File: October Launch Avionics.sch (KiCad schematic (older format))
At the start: 18 parts, among them IC1 MPU-6050, IC2 790, IC3 BMP384, J1 U.FL-R-SMT_01_, J2 MEM2075-00-140-01-A, U1 ESP32-WROOM-32D

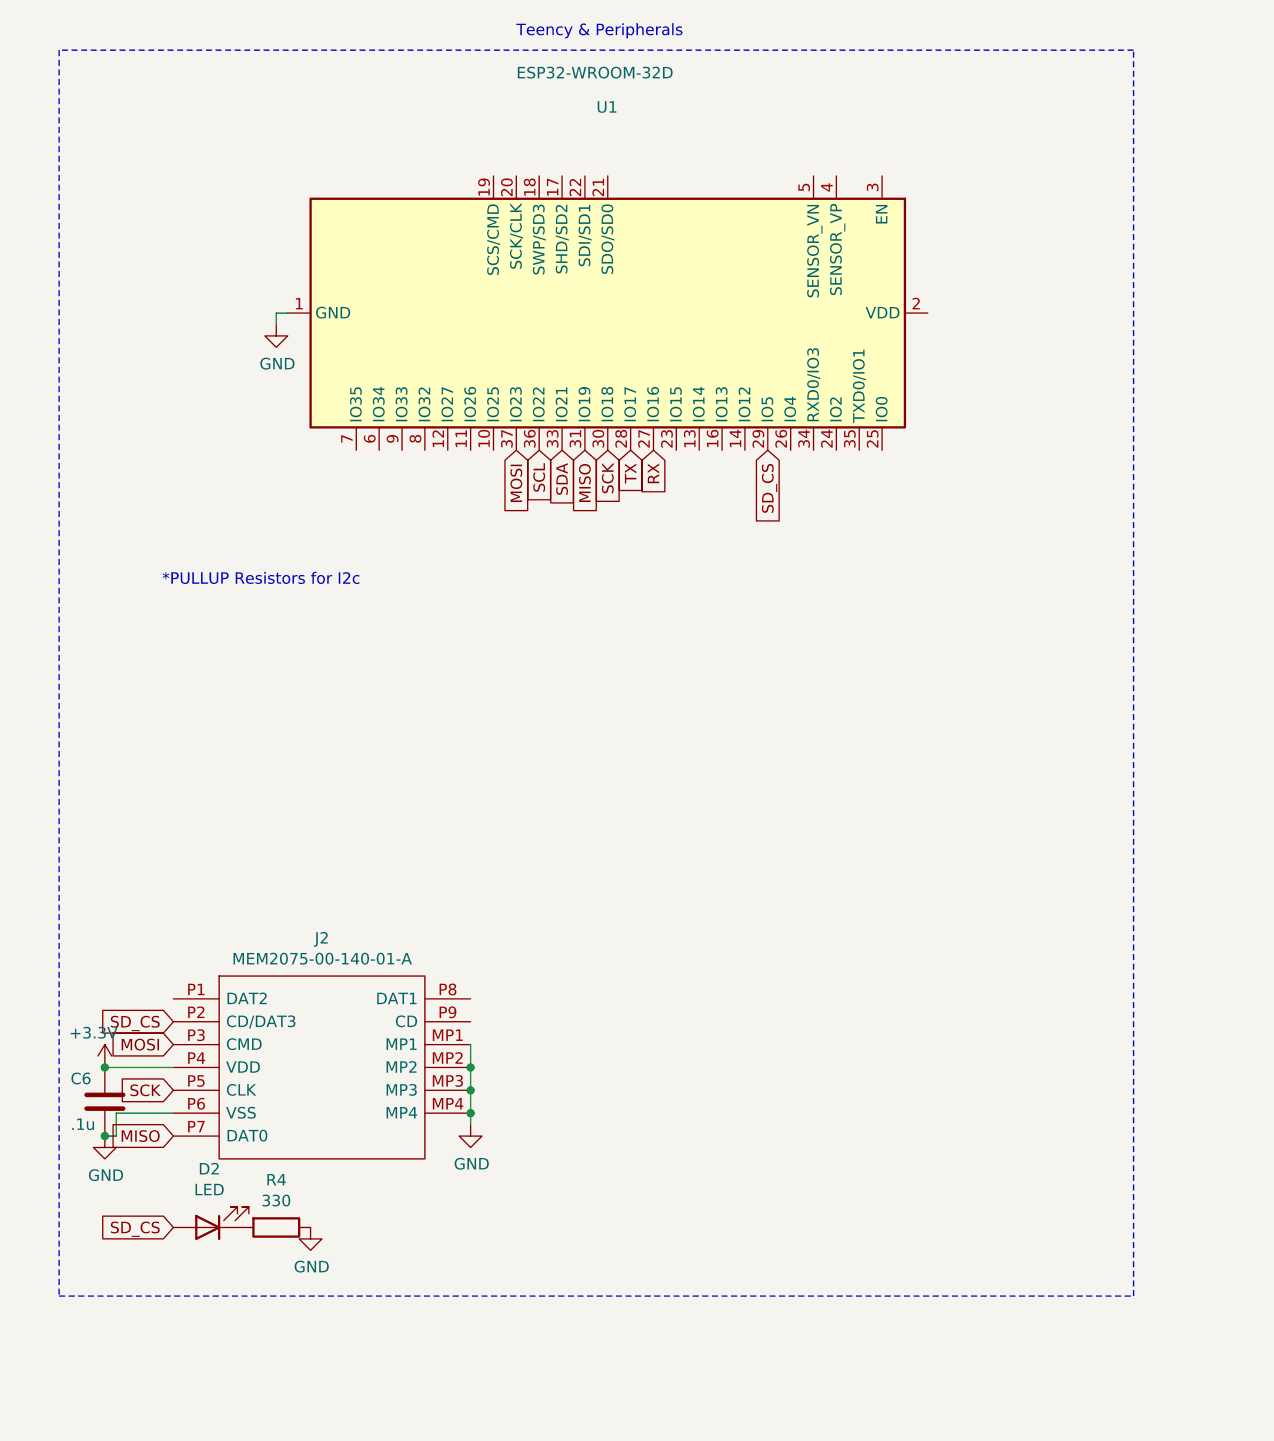
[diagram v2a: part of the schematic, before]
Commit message: Added reset button
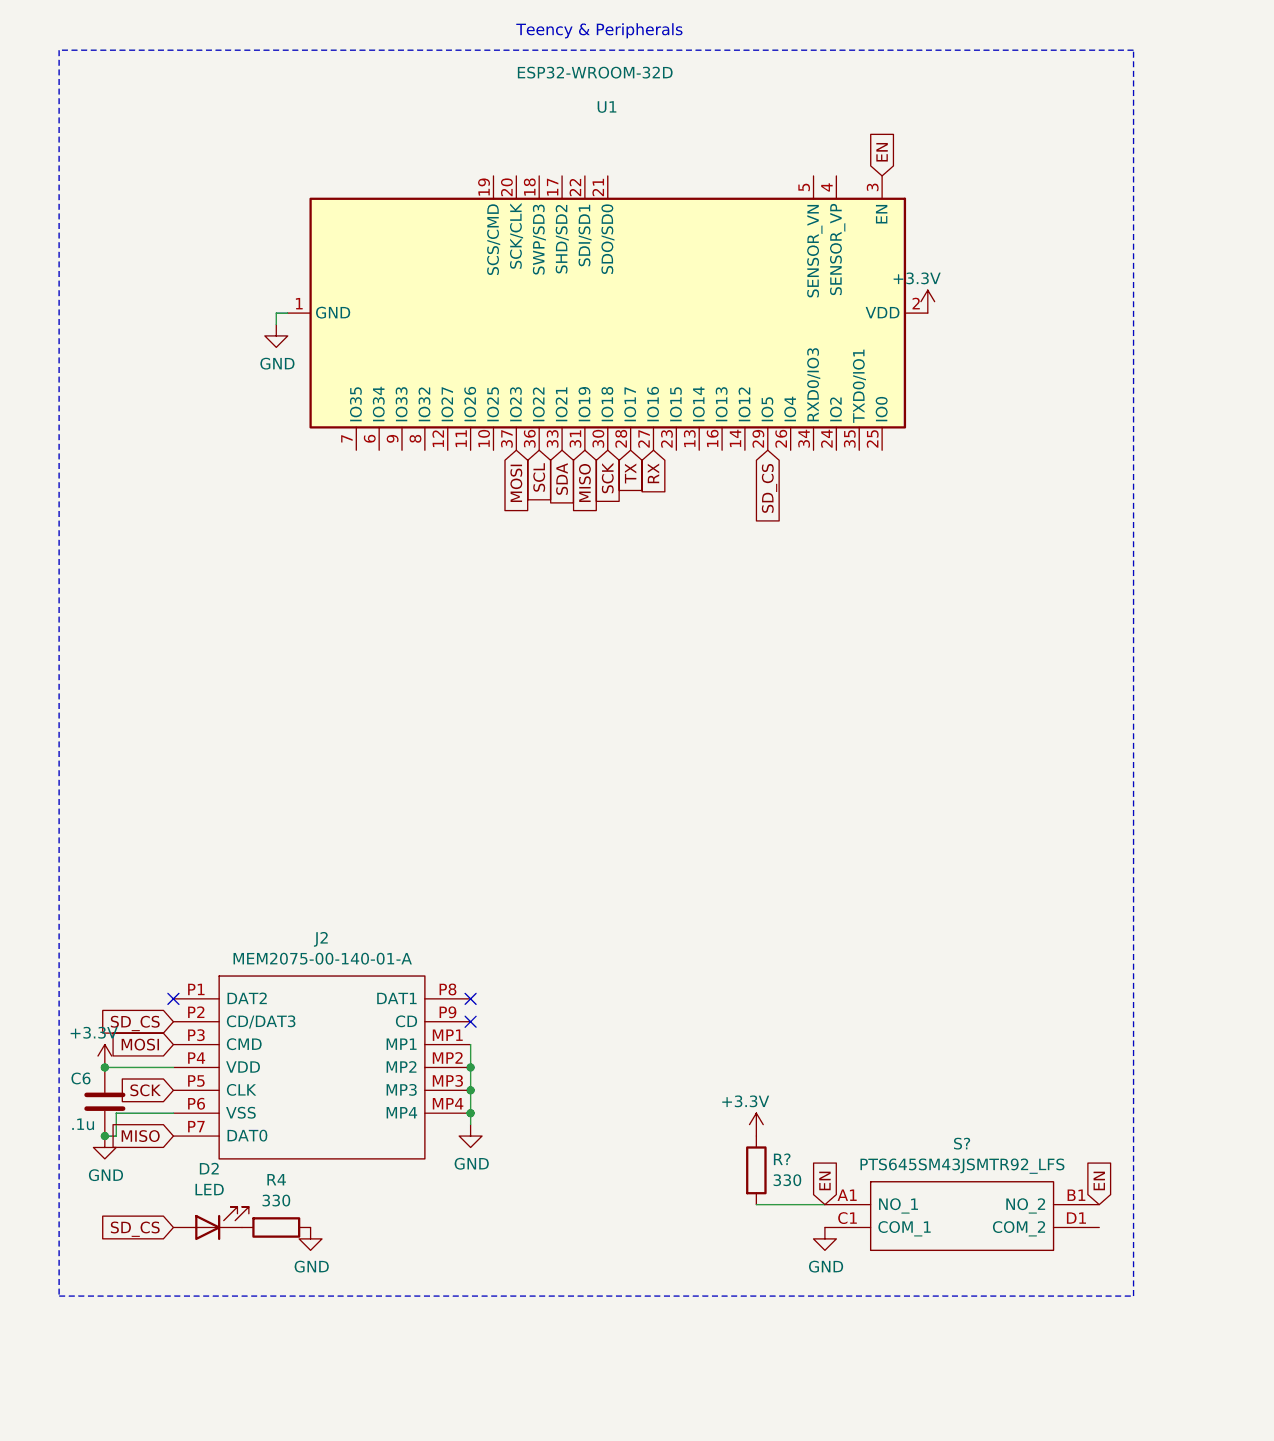
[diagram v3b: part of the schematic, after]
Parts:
- added R?: 330, symbol Device:R
- added S?: PTS645SM43JSMTR92_LFS, PTS645SM43JSMTR92LFS, symbol SamacSys_Parts:PTS645SM43JSMTR92_LFS
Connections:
- net +3V3: now also U1.2 (VDD), R?.1
- net GND: now also S?.C1 (COM_1)
- net EN: now reaches U1.3 (EN)
- net EN: now also R?.2, S?.A1 (NO_1), S?.B1 (NO_2)
- no-connect marks 23 -> 26
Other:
- note removed: "*PULLUP Resistors for I2c"
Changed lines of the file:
@@
 Text GLabel 1500 4550 1    50   Input ~ 0
 SCL
-Text Notes 6450 3150 0    50   ~ 0
-*PULLUP Resistors for I2c
 $Comp
 L power:+3.3V #PWR015
@@
 Text GLabel 9100 2550 3    50   Input ~ 0
 SD_CS
+NoConn ~ 6500 4950
+NoConn ~ 7800 5050
+NoConn ~ 7800 4950
+$Comp
+L power:+3.3V #PWR?
+U 1 1 61080F74
+P 9800 1950
+F 0 "#PWR?" H 9800 1800 50  0001 C CNN
+F 1 "+3.3V" H 9750 2100 50  0000 C CNN
+F 2 "" H 9800 1950 50  0001 C CNN
+F 3 "" H 9800 1950 50  0001 C CNN
+	1    9800 1950
+	1    0    0    -1
+$EndComp
+Text GLabel 9600 1350 1    50   Input ~ 0
+EN
+Text GLabel 10550 5850 1    50   Input ~ 0
+EN
+$Comp
+L SamacSys_Parts:PTS645SM43JSMTR92_LFS S?
+U 1 1 61081AFF
+P 9350 5850
+F 0 "S?" H 9950 6115 50  0000 C CNN
+F 1 "PTS645SM43JSMTR92_LFS" H 9950 6024 50  0000 C CNN
+F 2 "PTS645SM43JSMTR92LFS" H 10400 5950 50  0001 L CNN
+F 3 "https://www.mouser.tw/ProductDetail/CK/PTS645SM43JSMTR92-LFS?qs=TiOZkKH1s2T1Y3ae9C0wSg%3D%3D" H 10400 5850 50  0001 L CNN
+F 4 "Tactile Switches 50mA 12VDC, SPST NO, 160 gf, 4.3mm H, SMT J-type" H 10400 5750 50  0001 L CNN "Description"
+F 5 "4.8" H 10400 5650 50  0001 L CNN "Height"
+F 6 "611-SM43JSMTR92LFS" H 10400 5550 50  0001 L CNN "Mouser Part Number"
+F 7 "https://www.mouser.co.uk/ProductDetail/CK/PTS645SM43JSMTR92-LFS?qs=TiOZkKH1s2T1Y3ae9C0wSg%3D%3D" H 10400 5450 50  0001 L CNN "Mouser Price/Stock"
+F 8 "C & K COMPONENTS" H 10400 5350 50  0001 L CNN "Manufacturer_Name"
+F 9 "PTS645SM43JSMTR92 LFS" H 10400 5250 50  0001 L CNN "Manufacturer_Part_Number"
+	1    9350 5850
+	1    0    0    -1
+$EndComp
+$Comp
+L power:GND #PWR?
+U 1 1 61083EA1
+P 9350 5950
+F 0 "#PWR?" H 9350 5700 50  0001 C CNN
+F 1 "GND" H 9355 5777 50  0000 C CNN
+F 2 "" H 9350 5950 50  0001 C CNN
+F 3 "" H 9350 5950 50  0001 C CNN
+	1    9350 5950
+	1    0    0    -1
+$EndComp
+Text GLabel 9350 5850 1    50   Input ~ 0
+EN
+$Comp
+L Device:R R?
+U 1 1 61088122
+P 9050 5700
+F 0 "R?" H 9120 5746 50  0000 L CNN
+F 1 "330" H 9120 5655 50  0000 L CNN
+F 2 "" V 8980 5700 50  0001 C CNN
+F 3 "~" H 9050 5700 50  0001 C CNN
+	1    9050 5700
+	1    0    0    -1
+$EndComp
+$Comp
+L power:+3.3V #PWR?
+U 1 1 61088AE9
+P 9050 5550
+F 0 "#PWR?" H 9050 5400 50  0001 C CNN
+F 1 "+3.3V" H 9000 5700 50  0000 C CNN
+F 2 "" H 9050 5550 50  0001 C CNN
+F 3 "" H 9050 5550 50  0001 C CNN
+	1    9050 5550
+	1    0    0    -1
+$EndComp
+Wire Wire Line
+	9050 5850 9350 5850
 $EndSCHEMATC

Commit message: fixed component symbols
component symbols were incorrect, they should now be correct
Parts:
- added C7, C8: CP, symbol Device:CP
- added D3: D, symbol Device:D
- added L1: L, symbol Device:L
- added U2: LM2596S-5, Package_TO_SOT_SMD:TO-263-5_TabPin3, symbol Regulator_Switching:LM2596S-5
- gave numbers to parts that had none: 2
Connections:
- net GND: now also C7.2, C8.2, D3.2 (A), U2.3 (GND), U2.5 (~ON~/OFF)
- new net: C7.1, U2.1 (VIN)
- new net: D3.1 (K), L1.1, U2.2 (OUT)
- new net +5V: C8.1, L1.2, U2.4 (FB)
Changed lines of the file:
@@
 NoConn ~ 7800 4950
 $Comp
-L power:+3.3V #PWR?
+L power:+3.3V #PWR0102
 U 1 1 61080F74
 P 9800 1950
-F 0 "#PWR?" H 9800 1800 50  0001 C CNN
+F 0 "#PWR0102" H 9800 1800 50  0001 C CNN
 F 1 "+3.3V" H 9750 2100 50  0000 C CNN
 F 2 "" H 9800 1950 50  0001 C CNN
@@
 EN
 $Comp
-L SamacSys_Parts:PTS645SM43JSMTR92_LFS S?
+L SamacSys_Parts:PTS645SM43JSMTR92_LFS S1
 U 1 1 61081AFF
 P 9350 5850
-F 0 "S?" H 9950 6115 50  0000 C CNN
+F 0 "S1" H 9950 6115 50  0000 C CNN
 F 1 "PTS645SM43JSMTR92_LFS" H 9950 6024 50  0000 C CNN
 F 2 "PTS645SM43JSMTR92LFS" H 10400 5950 50  0001 L CNN
@@
 $EndComp
 $Comp
-L power:GND #PWR?
+L power:GND #PWR0103
 U 1 1 61083EA1
 P 9350 5950
-F 0 "#PWR?" H 9350 5700 50  0001 C CNN
+F 0 "#PWR0103" H 9350 5700 50  0001 C CNN
 F 1 "GND" H 9355 5777 50  0000 C CNN
 F 2 "" H 9350 5950 50  0001 C CNN
@@
 EN
 $Comp
-L Device:R R?
+L Device:R R5
 U 1 1 61088122
 P 9050 5700
-F 0 "R?" H 9120 5746 50  0000 L CNN
+F 0 "R5" H 9120 5746 50  0000 L CNN
 F 1 "330" H 9120 5655 50  0000 L CNN
 F 2 "" V 8980 5700 50  0001 C CNN
@@
 $EndComp
 $Comp
-L power:+3.3V #PWR?
+L power:+3.3V #PWR0104
 U 1 1 61088AE9
 P 9050 5550
-F 0 "#PWR?" H 9050 5400 50  0001 C CNN
+F 0 "#PWR0104" H 9050 5400 50  0001 C CNN
 F 1 "+3.3V" H 9000 5700 50  0000 C CNN
 F 2 "" H 9050 5550 50  0001 C CNN
@@
 Wire Wire Line
 	9050 5850 9350 5850
+$Comp
+L Regulator_Switching:LM2596S-5 U2
+U 1 1 61015F13
+P 2800 1250
+F 0 "U2" H 2800 1617 50  0000 C CNN
+F 1 "LM2596S-5" H 2800 1526 50  0000 C CNN
+F 2 "Package_TO_SOT_SMD:TO-263-5_TabPin3" H 2850 1000 50  0001 L CIN
+F 3 "http://www.ti.com/lit/ds/symlink/lm2596.pdf" H 2800 1250 50  0001 C CNN
+	1    2800 1250
+	1    0    0    -1
+$EndComp
+$Comp
+L power:+5V #PWR0107
+U 1 1 6102E3B5
+P 4150 1150
+F 0 "#PWR0107" H 4150 1000 50  0001 C CNN
+F 1 "+5V" V 4165 1278 50  0000 L CNN
+F 2 "" H 4150 1150 50  0001 C CNN
+F 3 "" H 4150 1150 50  0001 C CNN
+	1    4150 1150
+	0    1    1    0
+$EndComp
+$Comp
+L Device:L L1
+U 1 1 610792E4
+P 3500 1350
+F 0 "L1" V 3690 1350 50  0000 C CNN
+F 1 "L" V 3599 1350 50  0000 C CNN
+F 2 "" H 3500 1350 50  0001 C CNN
+F 3 "~" H 3500 1350 50  0001 C CNN
+	1    3500 1350
+	0    -1   -1   0
+$EndComp
+$Comp
+L Device:D D3
+U 1 1 61076105
+P 3350 1500
+F 0 "D3" V 3304 1580 50  0000 L CNN
+F 1 "D" V 3395 1580 50  0000 L CNN
+F 2 "" H 3350 1500 50  0001 C CNN
+F 3 "~" H 3350 1500 50  0001 C CNN
+	1    3350 1500
+	0    1    1    0
+$EndComp
+Connection ~ 3350 1650
+$Comp
+L power:GND #PWR0105
+U 1 1 61028B2E
+P 1600 1650
+F 0 "#PWR0105" H 1600 1400 50  0001 C CNN
+F 1 "GND" V 1605 1522 50  0000 R CNN
+F 2 "" H 1600 1650 50  0001 C CNN
+F 3 "" H 1600 1650 50  0001 C CNN
+	1    1600 1650
+	0    1    1    0
+$EndComp
+Wire Wire Line
+	2300 1350 2300 1650
+Connection ~ 2300 1650
+Wire Wire Line
+	2300 1650 2800 1650
+Wire Wire Line
+	2800 1550 2800 1650
+Connection ~ 2800 1650
+Wire Wire Line
+	2800 1650 3350 1650
+Wire Wire Line
+	3300 1350 3350 1350
+Connection ~ 3350 1350
+Wire Wire Line
+	3650 1350 3700 1350
+Wire Wire Line
+	3700 1350 3700 1150
+Connection ~ 3700 1150
+Wire Wire Line
+	3700 1150 3300 1150
+Wire Wire Line
+	3700 1150 4150 1150
+$Comp
+L power:GND #PWR0106
+U 1 1 610A5901
+P 4100 1650
+F 0 "#PWR0106" H 4100 1400 50  0001 C CNN
+F 1 "GND" V 4105 1522 50  0000 R CNN
+F 2 "" H 4100 1650 50  0001 C CNN
+F 3 "" H 4100 1650 50  0001 C CNN
+	1    4100 1650
+	0    -1   -1   0
+$EndComp
+$Comp
+L Device:CP C8
+U 1 1 610A7BB2
+P 3700 1500
+F 0 "C8" H 3818 1546 50  0000 L CNN
+F 1 "CP" H 3818 1455 50  0000 L CNN
+F 2 "" H 3738 1350 50  0001 C CNN
+F 3 "~" H 3700 1500 50  0001 C CNN
+	1    3700 1500
+	1    0    0    -1
+$EndComp
+Wire Wire Line
+	3350 1650 3700 1650
+Connection ~ 3700 1350
+Connection ~ 3700 1650
+Wire Wire Line
+	3700 1650 4100 1650
+$Comp
+L Device:CP C7
+U 1 1 610AC176
+P 2050 1400
+F 0 "C7" H 2168 1446 50  0000 L CNN
+F 1 "CP" H 2168 1355 50  0000 L CNN
+F 2 "" H 2088 1250 50  0001 C CNN
+F 3 "~" H 2050 1400 50  0001 C CNN
+	1    2050 1400
+	1    0    0    -1
+$EndComp
+Wire Wire Line
+	1600 1150 2050 1150
+Wire Wire Line
+	1600 1650 2050 1650
+Wire Wire Line
+	2050 1250 2050 1150
+Connection ~ 2050 1150
+Wire Wire Line
+	2050 1150 2300 1150
+Wire Wire Line
+	2050 1550 2050 1650
+Connection ~ 2050 1650
+Wire Wire Line
+	2050 1650 2300 1650
 $EndSCHEMATC
